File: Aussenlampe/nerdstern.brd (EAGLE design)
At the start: 60 x 50 mm, 10 parts, among them K1 G6RS

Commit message: add optocopler, wirin still questionable
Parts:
- added OK1: CNY17, optocoupler:DIL06
- moved C1 6.32 mm to (44.0, 15.0)
- moved D1 6.32 mm to (48.0, 11.0)
- moved D2 6.32 mm to (40.0, 11.0)
- moved D3 6.32 mm to (48.0, 19.0)
- moved D4 6.32 mm to (40.0, 19.0)
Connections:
- removed net GND: K1.2, X3.1
- new net N$10: OK1.1, X3.1
- new net N$11: OK1.2, X3.2
- new net N$12: K1.2, OK1.4
- net N$6: now also OK1.6; no longer X3.2
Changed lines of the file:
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@@
 <elements>
 <element name="TR1" library="trafo" package="EE20-1" value="" x="34.6" y="36.7" rot="R270"/>
-<element name="D1" library="diode" package="DO35-7" value="1N4148DO35-7" x="42" y="9" rot="R225"/>
-<element name="D2" library="diode" package="DO35-7" value="1N4148DO35-7" x="34" y="9" rot="R315"/>
-<element name="D3" library="diode" package="DO35-7" value="1N4148DO35-7" x="42" y="17" rot="R135"/>
-<element name="D4" library="diode" package="DO35-7" value="1N4148DO35-7" x="34" y="17" rot="R45"/>
-<element name="C1" library="rcl" package="E2-5" value="" x="38" y="13" rot="R270"/>
+<element name="D1" library="diode" package="DO35-7" value="1N4148DO35-7" x="48" y="11" rot="R225"/>
+<element name="D2" library="diode" package="DO35-7" value="1N4148DO35-7" x="40" y="11" rot="R315"/>
+<element name="D3" library="diode" package="DO35-7" value="1N4148DO35-7" x="48" y="19" rot="R135"/>
+<element name="D4" library="diode" package="DO35-7" value="1N4148DO35-7" x="40" y="19" rot="R45"/>
+<element name="C1" library="rcl" package="E2-5" value="" x="44" y="15" rot="R270"/>
 <element name="K1" library="relay" package="G6RS" value="G6RS" x="16" y="28" rot="R90">
 <attribute name="OC_NEWARK" value="unknown" x="16" y="28" size="1.778" layer="27" rot="R90" display="off"/>
@@
 <attribute name="OC_FARNELL" value="unknown" x="21.55" y="5.33" size="1.778" layer="27" display="off"/>
 </element>
+<element name="OK1" library="optocoupler" package="DIL06" value="CNY17" x="29" y="18">
+<attribute name="OC_NEWARK" value="05M4044" x="29" y="18" size="1.778" layer="27" display="off"/>
+<attribute name="MPN" value="CNY17-1" x="29" y="18" size="1.778" layer="27" display="off"/>
+<attribute name="MF" value="" x="29" y="18" size="1.778" layer="27" display="off"/>
+<attribute name="OC_FARNELL" value="1045399" x="29" y="18" size="1.778" layer="27" display="off"/>
+</element>
 </elements>
 <signals>
@@
 <contactref element="TR1" pad="4"/>
 <contactref element="K1" pad="S"/>
-<wire x1="54" y1="35" x2="12.19" y2="39.43" width="0" layer="19" extent="1-1"/>
 <wire x1="27.107" y1="44.193" x2="54" y2="35" width="0" layer="19" extent="1-1"/>
+<wire x1="12.19" y1="39.43" x2="27.107" y2="44.193" width="0" layer="19" extent="1-1"/>
 </signal>
 <signal name="N$2">
@@
 <contactref element="X1" pad="1"/>
 <contactref element="X2" pad="1"/>
-<wire x1="54" y1="40.0038" x2="42.093" y2="44.193" width="0" layer="19" extent="1-1"/>
+<wire x1="42.093" y1="44.193" x2="54" y2="40.0038" width="0" layer="19" extent="1-1"/>
 <wire x1="6" y1="29.9962" x2="42.093" y2="44.193" width="0" layer="19" extent="1-1"/>
 </signal>
@@
 <contactref element="D1" pad="C"/>
 <contactref element="D3" pad="C"/>
-<wire x1="44.694075" y1="11.694075" x2="44.694075" y2="14.305921875" width="0" layer="19" extent="1-1"/>
-<wire x1="37.1146" y1="29.207" x2="44.694075" y2="11.694075" width="0" layer="19" extent="1-1"/>
+<wire x1="50.694075" y1="16.305921875" x2="37.1146" y2="29.207" width="0" layer="19" extent="1-1"/>
+<wire x1="50.694075" y1="13.694075" x2="50.694075" y2="16.305921875" width="0" layer="19" extent="1-1"/>
 </signal>
 <signal name="N$5">
@@
 <contactref element="D4" pad="A"/>
 <contactref element="K1" pad="1"/>
-<wire x1="36.694075" y1="19.694075" x2="39.305921875" y2="19.694075" width="0" layer="19" extent="1-1"/>
-<wire x1="38" y1="14.016" x2="36.694075" y2="19.694075" width="0" layer="19" extent="1-1"/>
-<wire x1="19.81" y1="15.3" x2="38" y2="14.016" width="0" layer="19" extent="1-1"/>
+<wire x1="45.305921875" y1="21.694075" x2="42.694075" y2="21.694075" width="0" layer="19" extent="1-16"/>
+<wire x1="44" y1="16.016" x2="45.305921875" y2="21.694075" width="0" layer="19" extent="1-1"/>
+<wire x1="19.81" y1="15.3" x2="42.694075" y2="21.694075" width="0" layer="19" extent="1-1"/>
 </signal>
 <signal name="N$6">
@@
 <contactref element="D1" pad="A"/>
 <contactref element="D2" pad="A"/>
-<contactref element="X3" pad="2"/>
-<wire x1="38" y1="11.984" x2="39.305921875" y2="6.305921875" width="0" layer="19" extent="1-1"/>
-<wire x1="36.694075" y1="6.305921875" x2="38" y2="11.984" width="0" layer="19" extent="1-1"/>
-<wire x1="24.0646" y1="5.33" x2="36.694075" y2="6.305921875" width="0" layer="19" extent="1-1"/>
+<contactref element="OK1" pad="6"/>
+<wire x1="45.305921875" y1="8.305921875" x2="44" y2="13.984" width="0" layer="19" extent="1-1"/>
+<wire x1="42.694075" y1="8.305921875" x2="45.305921875" y2="8.305921875" width="0" layer="19" extent="1-1"/>
+<wire x1="26.46" y1="21.81" x2="44" y2="13.984" width="0" layer="19" extent="1-1"/>
 </signal>
 <signal name="N$7">
@@
 <contactref element="D2" pad="C"/>
 <contactref element="TR1" pad="6"/>
-<wire x1="31.305921875" y1="11.694075" x2="31.305921875" y2="14.305921875" width="0" layer="19" extent="1-1"/>
-<wire x1="32.0854" y1="29.207" x2="31.305921875" y2="11.694075" width="0" layer="19" extent="1-1"/>
-</signal>
-<signal name="GND">
-<contactref element="K1" pad="2"/>
-<contactref element="X3" pad="1"/>
-<wire x1="19.0354" y1="5.33" x2="12.19" y2="15.3" width="0" layer="19" extent="1-1"/>
+<wire x1="37.305921875" y1="16.305921875" x2="32.0854" y2="29.207" width="0" layer="19" extent="1-1"/>
+<wire x1="37.305921875" y1="13.694075" x2="37.305921875" y2="16.305921875" width="0" layer="19" extent="1-1"/>
 </signal>
 <signal name="N$8">
@@
 </polygon>
 </signal>
+<signal name="N$10">
+<contactref element="OK1" pad="1"/>
+<contactref element="X3" pad="1"/>
+<wire x1="19.0354" y1="5.33" x2="26.46" y2="14.19" width="0" layer="19" extent="1-1"/>
+</signal>
+<signal name="N$11">
+<contactref element="OK1" pad="2"/>
+<contactref element="X3" pad="2"/>
+<wire x1="24.0646" y1="5.33" x2="29" y2="14.19" width="0" layer="19" extent="1-1"/>
+</signal>
+<signal name="N$12">
+<contactref element="K1" pad="2"/>
+<contactref element="OK1" pad="4"/>
+<wire x1="12.19" y1="15.3" x2="31.54" y2="21.81" width="0" layer="19" extent="1-1"/>
+</signal>
 </signals>

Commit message: routing and some repositioning of parts
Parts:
- moved OK1 12.1 mm to (34.0, 7.00), turned to 270 degrees
- moved C1 5.10 mm to (49.0, 16.0)
- moved D1 5.10 mm to (53.0, 12.0)
- moved D2 5.10 mm to (45.0, 12.0)
- moved D3 5.10 mm to (53.0, 20.0)
- moved D4 5.10 mm to (45.0, 20.0)
- moved TR1 4.12 mm to (33.6, 32.7)
- moved X3 3.16 mm to (18.6, 4.33)
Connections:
- net N$3: now also X2.3; no longer X2.1
- net N$8: now also X2.1; no longer X2.3
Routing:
- net N$3: track 0.00 -> 57.6 mm
- net N$5: track 0.00 -> 52.7 mm
- net N$8: track 0.00 -> 50.5 mm
- net N$1: track 0.00 -> 44.3 mm
- net N$12: track 0.00 -> 33.9 mm
- net N$4: track 0.00 -> 28.4 mm
- net N$7: track 0.00 -> 19.6 mm
- net N$6: track 0.00 -> 18.8 mm
- net N$10: track 0.00 -> 17.9 mm
- net N$2: track 0.00 -> 14.1 mm
- net N$11: track 0.00 -> 11.3 mm
- added copper zone on layer 16, net N$13
- removed copper zone on layer 16, net GND2

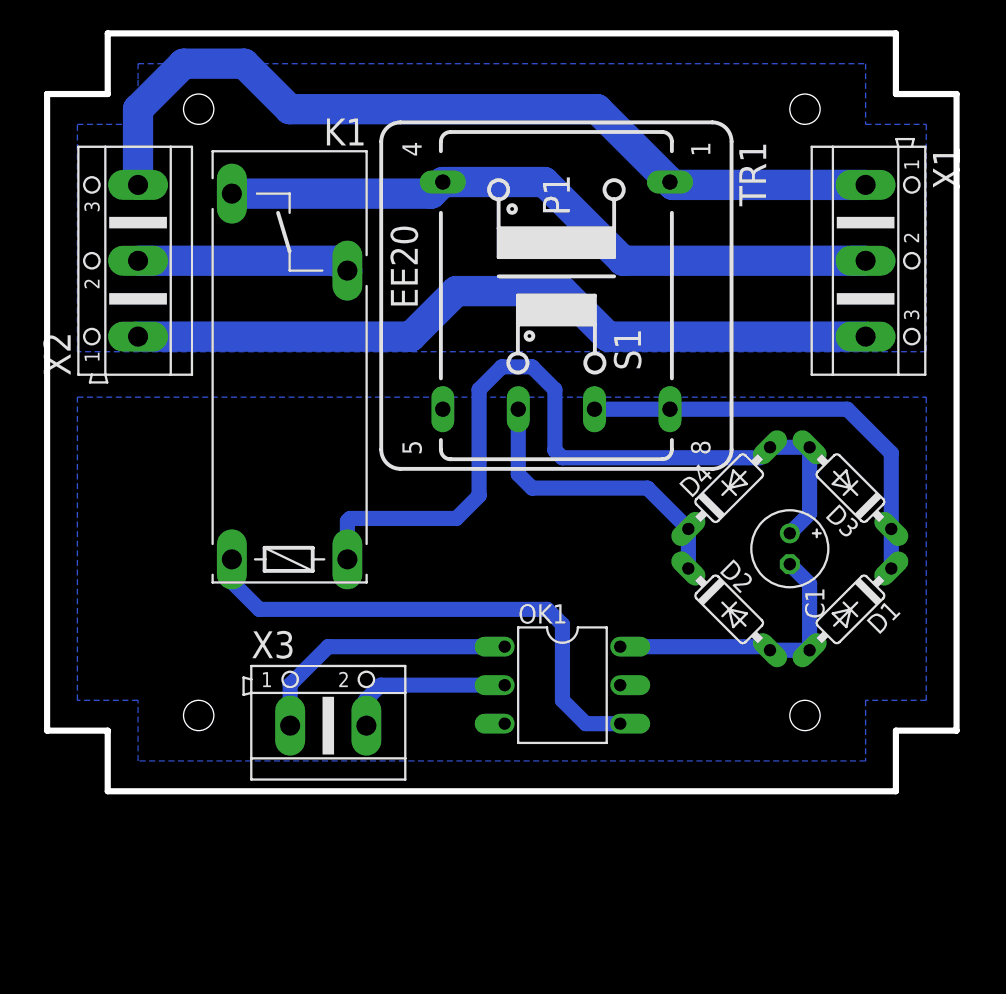
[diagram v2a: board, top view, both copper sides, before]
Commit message: schaltplan korrigiert
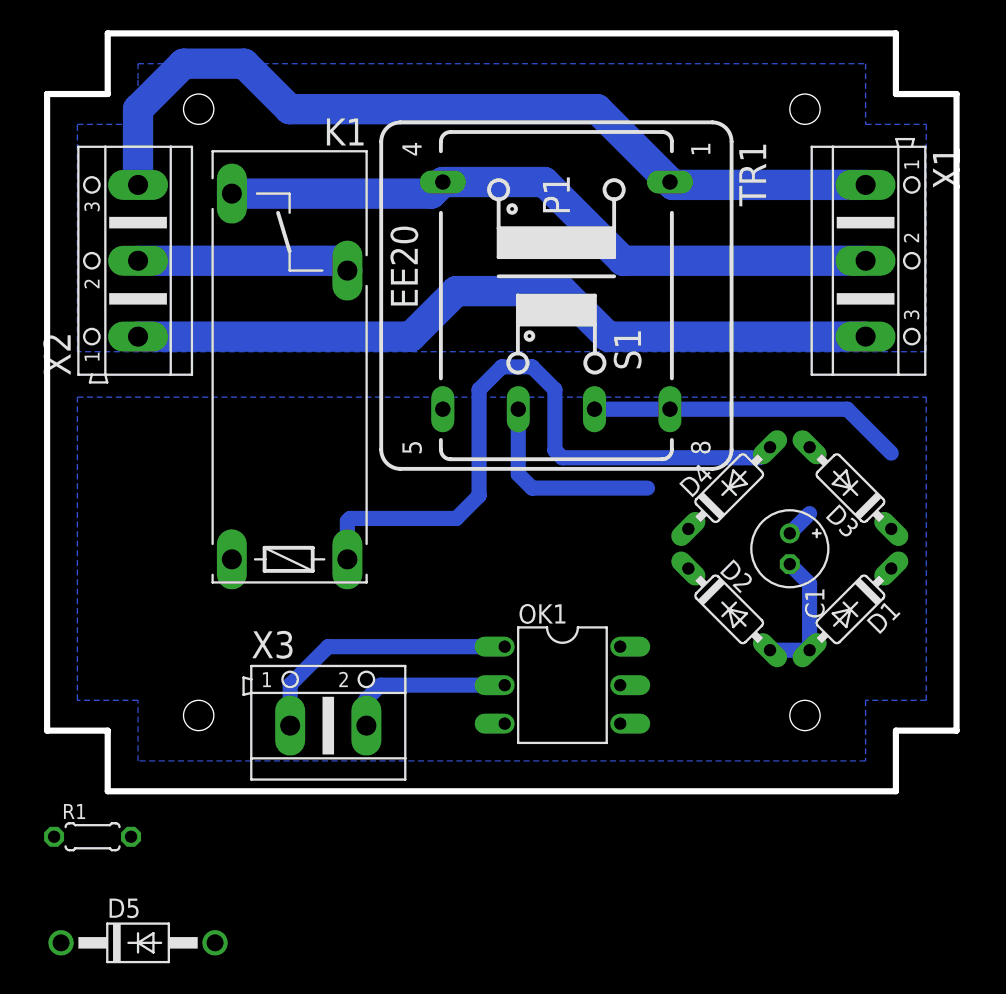
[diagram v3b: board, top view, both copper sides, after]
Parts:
- added D5: 1N4004, diode:DO41-10
- added R1: 1M, rcl:0204/5
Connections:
- removed net N$6: C1.-, D1.A, D2.A, OK1.6
- new net GND: C1.-, D1.A, D2.A, OK1.4, R1.2
- new net N$14: OK1.6, R1.1
- net N$12: now also D5.A, OK1.5; no longer OK1.4
- net N$4: now also D3.A; no longer D3.C
- net N$5: now also D3.C, D4.C, D5.C; no longer D3.A, D4.A
- net N$7: now also D4.A; no longer D4.C
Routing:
- net N$12: track 33.9 -> 0.00 mm
- net N$6: track 18.8 -> 0.00 mm
- net GND: track 0.00 -> 9.16 mm
- net N$5: track 52.7 -> 44.7 mm
- net N$4: track 28.4 -> 20.8 mm
- net N$7: track 19.6 -> 13.2 mm
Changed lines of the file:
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@@
 <attribute name="OC_FARNELL" value="1045399" x="34" y="7" size="1.778" layer="27" rot="R270" display="off"/>
 </element>
+<element name="R1" library="rcl" package="0204/5" value="1M" x="3" y="-3"/>
+<element name="D5" library="diode" package="DO41-10" value="1N4004" x="6" y="-10"/>
 </elements>
 <signals>
@@
 <contactref element="TR1" pad="7"/>
 <contactref element="D1" pad="C"/>
-<contactref element="D3" pad="C"/>
-<wire x1="55.694075" y1="17.305921875" x2="55.694075" y2="14.694075" width="1" layer="16"/>
 <wire x1="36.1146" y1="25.207" x2="52.793" y2="25.207" width="1" layer="16"/>
 <wire x1="52.793" y1="25.207" x2="55.694075" y2="22.305925" width="1" layer="16"/>
-<wire x1="55.694075" y1="22.305925" x2="55.694075" y2="17.305921875" width="1" layer="16"/>
+<contactref element="D3" pad="A"/>
+<wire x1="52.793" y1="25.207" x2="50.305921875" y2="22.694075" width="0" layer="19" extent="16-16"/>
+<wire x1="55.694075" y1="14.694075" x2="55.694075" y2="22.305925" width="0" layer="19" extent="16-16"/>
 </signal>
 <signal name="N$5">
-<contactref element="D3" pad="A"/>
-<contactref element="C1" pad="+"/>
-<contactref element="D4" pad="A"/>
 <contactref element="K1" pad="1"/>
-<wire x1="47.694075" y1="22.694075" x2="50.305921875" y2="22.694075" width="1" layer="16"/>
-<wire x1="50.305921875" y1="22.694075" x2="50.305921875" y2="18.321921875" width="1" layer="16"/>
-<wire x1="50.305921875" y1="18.321921875" x2="49" y2="17.016" width="1" layer="16"/>
 <wire x1="19.81" y1="15.3" x2="19.81" y2="17.81" width="1" layer="16"/>
 <wire x1="19.81" y1="17.81" x2="20" y2="18" width="1" layer="16"/>
@@
 <wire x1="33.5" y1="22.5" x2="34" y2="22" width="1" layer="16"/>
 <wire x1="34" y1="22" x2="47" y2="22" width="1" layer="16"/>
-<wire x1="47" y1="22" x2="47.694075" y2="22.694075" width="1" layer="16"/>
+<contactref element="C1" pad="+"/>
+<contactref element="D3" pad="C"/>
+<contactref element="D4" pad="C"/>
+<wire x1="50.305921875" y1="18.321921875" x2="49" y2="17.016" width="1" layer="16"/>
+<contactref element="D5" pad="C"/>
+<wire x1="50.305921875" y1="18.321921875" x2="55.694075" y2="17.305921875" width="0" layer="19" extent="16-16"/>
+<wire x1="47" y1="22" x2="50.305921875" y2="18.321921875" width="0" layer="19" extent="16-16"/>
+<wire x1="42.305921875" y1="17.305921875" x2="47" y2="22" width="0" layer="19" extent="16-16"/>
+<wire x1="0.92" y1="-10" x2="19.81" y2="15.3" width="0" layer="19" extent="1-1"/>
 </signal>
-<signal name="N$6">
+<signal name="GND">
 <contactref element="C1" pad="-"/>
 <contactref element="D1" pad="A"/>
 <contactref element="D2" pad="A"/>
-<contactref element="OK1" pad="6"/>
 <wire x1="47.694075" y1="9.305921875" x2="50.305921875" y2="9.305921875" width="1" layer="16"/>
 <wire x1="50.305921875" y1="9.305921875" x2="50.305921875" y2="13.678078125" width="1" layer="16"/>
 <wire x1="50.305921875" y1="13.678078125" x2="49" y2="14.984" width="1" layer="16"/>
 <wire x1="47.694075" y1="9.305921875" x2="47.459996875" y2="9.54" width="1" layer="16"/>
-<wire x1="47.459996875" y1="9.54" x2="37.81" y2="9.54" width="1" layer="16"/>
+<contactref element="OK1" pad="4"/>
+<contactref element="R1" pad="2"/>
+<wire x1="37.81" y1="4.46" x2="47.459996875" y2="9.54" width="0" layer="19" extent="16-16"/>
+<wire x1="5.54" y1="-3" x2="37.81" y2="4.46" width="0" layer="19" extent="1-1"/>
 </signal>
 <signal name="N$7">
-<contactref element="D4" pad="C"/>
 <contactref element="D2" pad="C"/>
 <contactref element="TR1" pad="6"/>
-<wire x1="42.305921875" y1="17.305921875" x2="42.305921875" y2="14.694075" width="1" layer="16"/>
 <wire x1="31.0854" y1="25.207" x2="31.0854" y2="20.9146" width="1" layer="16"/>
 <wire x1="31.0854" y1="20.9146" x2="32" y2="20" width="1" layer="16"/>
 <wire x1="32" y1="20" x2="39.61184375" y2="20" width="1" layer="16"/>
-<wire x1="39.61184375" y1="20" x2="42.305921875" y2="17.305921875" width="1" layer="16"/>
+<contactref element="D4" pad="A"/>
+<wire x1="39.61184375" y1="20" x2="47.694075" y2="22.694075" width="0" layer="19" extent="16-16"/>
+<wire x1="42.305921875" y1="14.694075" x2="39.61184375" y2="20" width="0" layer="19" extent="16-16"/>
 </signal>
 <signal name="N$8">
@@
 <wire x1="21" y1="6" x2="22" y2="7" width="1" layer="16"/>
 <wire x1="22" y1="7" x2="30.19" y2="7" width="1" layer="16"/>
-</signal>
-<signal name="N$12">
-<contactref element="K1" pad="2"/>
-<contactref element="OK1" pad="4"/>
-<wire x1="12.19" y1="15.3" x2="12.19" y2="13.81" width="1" layer="16"/>
-<wire x1="12.19" y1="13.81" x2="14" y2="12" width="1" layer="16"/>
-<wire x1="14" y1="12" x2="33" y2="12" width="1" layer="16"/>
-<wire x1="33" y1="12" x2="34" y2="11" width="1" layer="16"/>
-<wire x1="34" y1="11" x2="34" y2="6" width="1" layer="16"/>
-<wire x1="34" y1="6" x2="35.54" y2="4.46" width="1" layer="16"/>
-<wire x1="35.54" y1="4.46" x2="37.81" y2="4.46" width="1" layer="16"/>
 </signal>
 <signal name="N$9">
@@
 </polygon>
 </signal>
+<signal name="N$14">
+<contactref element="R1" pad="1"/>
+<contactref element="OK1" pad="6"/>
+<wire x1="0.46" y1="-3" x2="37.81" y2="9.54" width="0" layer="19" extent="1-1"/>
+</signal>
+<signal name="N$12">
+<contactref element="K1" pad="2"/>
+<contactref element="OK1" pad="5"/>
+<contactref element="D5" pad="A"/>
+<wire x1="12.19" y1="15.3" x2="37.81" y2="7" width="0" layer="19" extent="1-1"/>
+<wire x1="11.08" y1="-10" x2="12.19" y2="15.3" width="0" layer="19" extent="1-1"/>
+</signal>
 </signals>

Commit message: routing
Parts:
- added R2: 1K, rcl:0204/5
- C1: value (none) -> 33u
- D1, D2, D3, D4: value 1N4148DO35-7 -> 1N4148
- D5: value 1N4004 -> 1N4001; device diode:DO41-10 -> diode:DO35-7
- moved R1 40.3 mm to (42.0, 7.00), turned to 270 degrees
- moved D5 36.4 mm to (35.0, 12.0), turned to 180 degrees
- moved C1 1.41 mm to (50.0, 17.0)
- moved D1 1.41 mm to (54.0, 13.0)
- moved D2 1.41 mm to (46.0, 13.0)
- moved D3 1.41 mm to (54.0, 21.0), turned to 315 degrees
- moved D4 1.41 mm to (46.0, 21.0), turned to 225 degrees
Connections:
- net N$8 renamed GND2
- new net N$15: R2.2, X3.1
- net N$10: now also R2.1; no longer X3.1
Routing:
- net N$12: track 0.00 -> 31.2 mm
- net GND: track 9.16 -> 22.1 mm
- net N$10: track 17.9 -> 6.84 mm
- net N$4: track 20.8 -> 30.2 mm
- net N$15: track 0.00 -> 6.67 mm
- net N$7: track 13.2 -> 17.7 mm
- net N$14: track 0.00 -> 4.19 mm
- net N$5: track 44.7 -> 43.7 mm
- added copper zone on layer 16, net GND
- added copper zone on layer 16, net GND2
- removed copper zone on layer 16, net N$13
- removed copper zone on layer 16, net N$9
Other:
- board text added: "netz39_nerdlicht CC-BY-SA netz39"
